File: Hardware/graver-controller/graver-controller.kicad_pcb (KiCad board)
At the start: 2 copper layers, 110 x 70 mm, 117 parts, among them J101 DC jack 5.5x2.1, J201 Handpiece, J301 USB-C, J302 SWD, J401 LCD XH 1x7, J402 NMJ6HCD2, Q101 DMP6023LE, Q201 IRLR3410, Q202 SI2309CDS, Q203 BSS123, SW301 BOOT0, SW302 RESET, SW401 EC11E15244G1, U101 LM5164DDAR, U102 AP2112K-3.3, U201 UCC27517DBVR, U202 TLV9062IDR, U301 STM32F411CEU6, U302 USBLC6-2SC6, U401 PESD5V0S2BT, Y301 25MHz 10pF

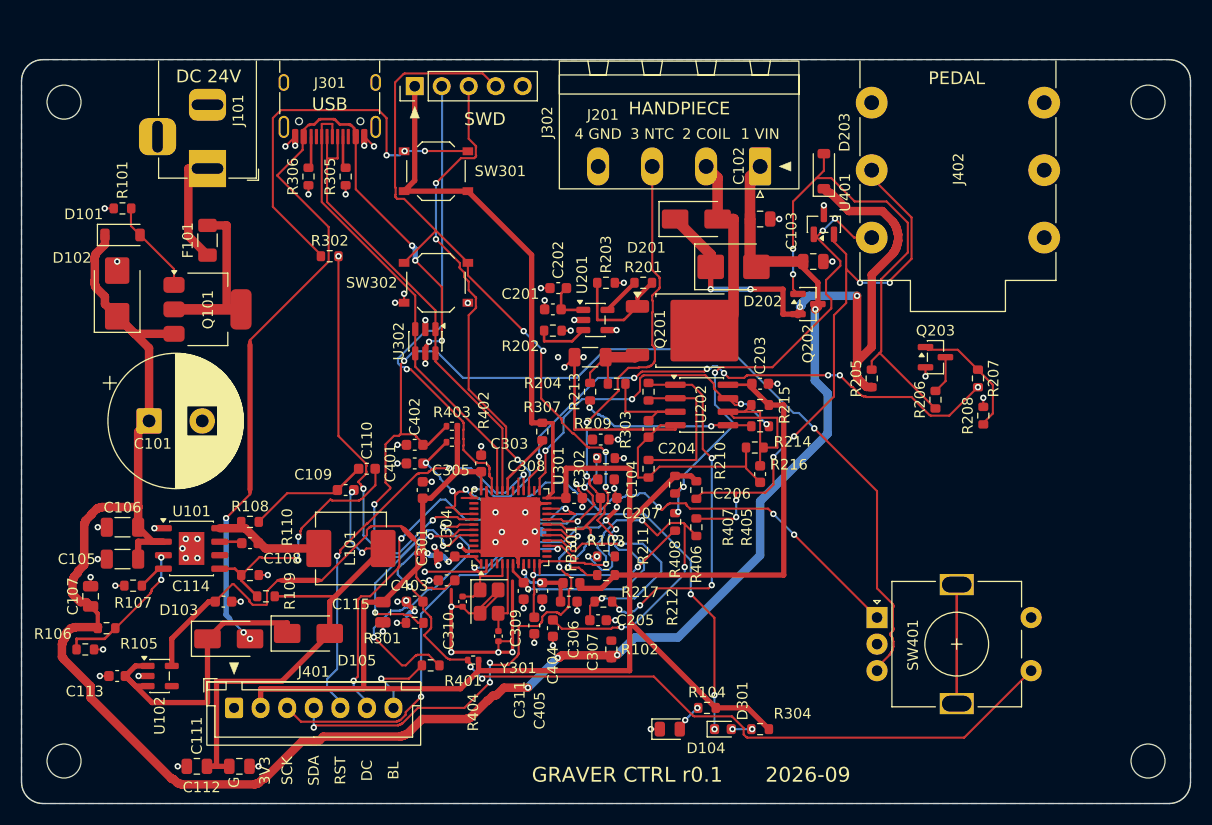
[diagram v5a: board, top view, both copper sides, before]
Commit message: hardware: GATE_IN, VCAP1 and VIN_SENSE drawn explicitly, 4 pad pairs left
copper.py: SIGNAL_EXPLICIT table drawn before the rails so the strike
signal (GATE_IN 16.7 mm), VCAP1 (10.8 mm) and the VIN_SENSE divider and
filter (20.2 mm, no via) get their lanes first. place.py: 3D model
substitutes for the QFN (EP 5.15 variant) and the two tact switches;
J301, SW401 and J402 have no library model anywhere and need
manufacturer STEP files before the enclosure export (README).

Repo board: 0 DRC errors, 0 parity, 4 unconnected pad pairs (I_SENSE x2,
DECAY_SLOW, LED_STAT), 202 vias. Budgets unchanged: USB 37.88/37.88
skew 0, flyback 21.4 mm, buck CIN 2.9/2.7 mm, Kelvin 1.15/1.23, sense
ground 5/5, no ADC net parallel to a switching net. +3V3 now 301 mm /
6 vias. An explicit I_SENSE trace was tried and reverted: it cost the
router GND and left 7 open.
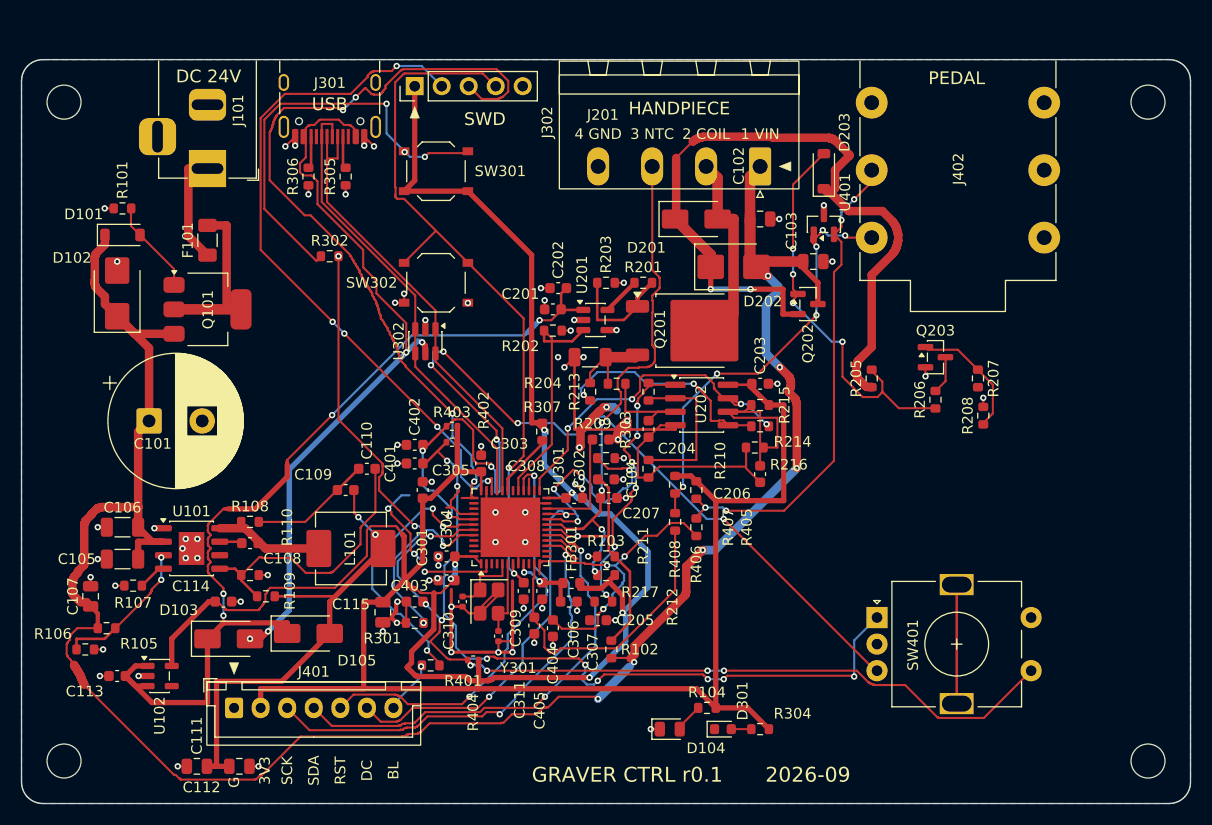
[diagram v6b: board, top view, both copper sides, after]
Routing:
- net +5V: track 33.2 -> 86.2 mm, vias 0 -> 4
- net DECAY_SLOW: track 52.4 -> 1.15 mm, vias 7 -> 0
- net LED_STAT: track 48.2 -> 6.56 mm, vias 5 -> 1
- net GND: track 193.6 -> 157.0 mm, vias 84 -> 82
- net SWCLK: track 52.2 -> 76.5 mm
- net +3V3: track 277.9 -> 301.0 mm, vias 2 -> 6
- net SWDIO: track 45.0 -> 66.3 mm, vias 1 -> 5
- net VIN_SENSE: track 3.15 -> 23.3 mm
- net I_SENSE: track 22.8 -> 3.01 mm, vias 2 -> 0
- net VBUS: track 89.6 -> 69.9 mm, vias 8 -> 4
- net NRST: track 87.8 -> 69.4 mm, vias 6 -> 2
- net ENC_A: track 59.8 -> 75.9 mm, vias 6 -> 8
- net GATE_IN: track 6.27 -> 21.8 mm
- net /Driver/CLAMP: track 57.9 -> 72.6 mm, vias 4 -> 2
- net Net-(U301-PB2): track 10.5 -> 22.3 mm, vias 3 -> 4
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
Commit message: hardware: scripted GND stitching, I_SENSE explicit, manual-track preservation
copper.py: every top-side GND pad (58) gets its own stub and via into
the pour, 17 edge stitching vias, a GND spine joining the F.Cu pieces;
the router no longer routes GND. Two real bugs fixed on the way: pad
numbers are not unique (SW302 has two pads '2', one was stitched twice
and one never) and the crystal's ground pads were tied to each other
and to nothing else. I_SENSE drawn explicitly (7.7 mm, no via).
manual.py + place.py --export-manual keep tracks drawn by hand in
pcbnew across regeneration (round trip verified, manual.json absent).

Repo board: 0 DRC errors, 0 parity, 5 unconnected pad pairs (GND x2
pour islands at C309/C205, ENC_B x2, +5V), 219 vias; one worse than
3406b49, the router's B.Cu tracks dice the pour. Budgets unchanged:
USB 37.88/37.88 skew 0, flyback 21.4 mm, buck CIN < 3 mm, Kelvin
1.15/1.23, sense ground 5/5, no ADC net parallel to a switching net.
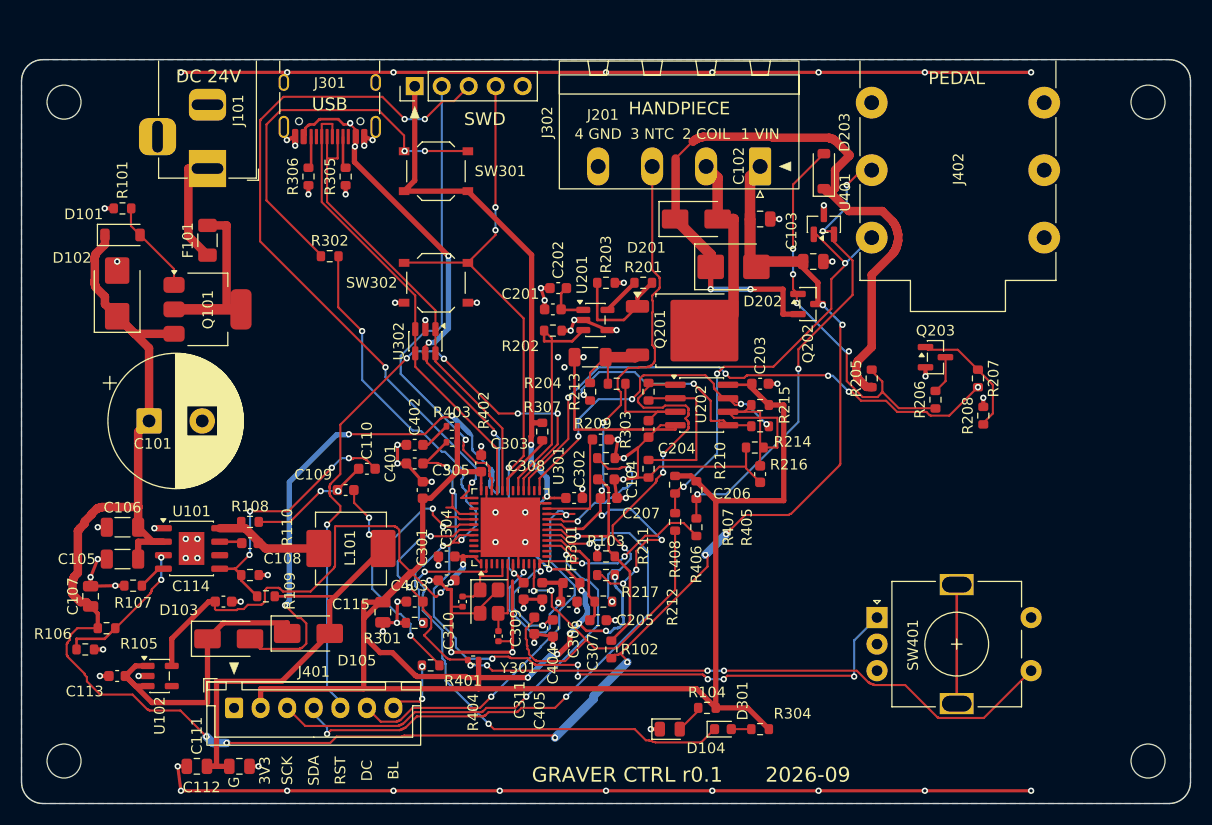
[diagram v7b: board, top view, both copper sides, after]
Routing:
- net GND: track 157.0 -> 308.6 mm, vias 82 -> 87
- net ENC_B: track 95.7 -> 5.62 mm, vias 8 -> 0
- net +5V: track 86.2 -> 33.2 mm, vias 4 -> 0
- net DECAY_SLOW: track 1.15 -> 53.1 mm, vias 0 -> 5
- net LED_STAT: track 6.56 -> 46.4 mm, vias 1 -> 2
- net VBUS: track 69.9 -> 96.9 mm, vias 4 -> 8
- net LCD_RST: track 39.8 -> 62.9 mm, vias 2 -> 5
- net SWDIO: track 66.3 -> 44.5 mm, vias 5 -> 1
- net NRST: track 69.4 -> 58.3 mm, vias 2 -> 4
- net LCD_MOSI: track 43.7 -> 54.6 mm, vias 2 -> 3
- net NTC: track 49.2 -> 59.4 mm, vias 4 -> 6
- net /MCU/VDDA: track 6.55 -> 16.3 mm
- net PEDAL_TIP: track 28.9 -> 37.2 mm, vias 0 -> 2
- net SWCLK: track 76.5 -> 68.3 mm
- net I_SENSE: track 3.01 -> 10.8 mm
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
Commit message: hardware: power widths honoured, GND closed, 3 pad pairs left
Two causes of the 0.2 mm power runs: the router necks a blocked wide
route down to --track-width and never widens it back, and the
.kicad_dru was never copied next to the scratch boards, so neither the
router nor the import gate saw the width rules (the real count was 237,
kicad-cli caps its report at 199). autoroute.py now routes one pass per
width floor (0.5, 0.3, then 0.2 mm signals), reads the floors from the
.kicad_dru and copies .kicad_pro + .kicad_dru beside every scratch
board; copper.py widths raised to the floors and checked.

Repo board with the width rules: 0 DRC errors, 0 parity, 3 unconnected
pad pairs (VDDA 2 mm, PB2 6 mm, +5V C201-D105 40 mm), 233 vias, all
GND pads on the main pour. Per-net minimum widths: VIN / CLAMP /
SHUNT_HI 0.5, COIL_NEG 1.0, +3V3 / +5V / VBUS / VDDA 0.3. Budgets
unchanged; +3V3 268 mm / 9 vias (was 300 / 13).
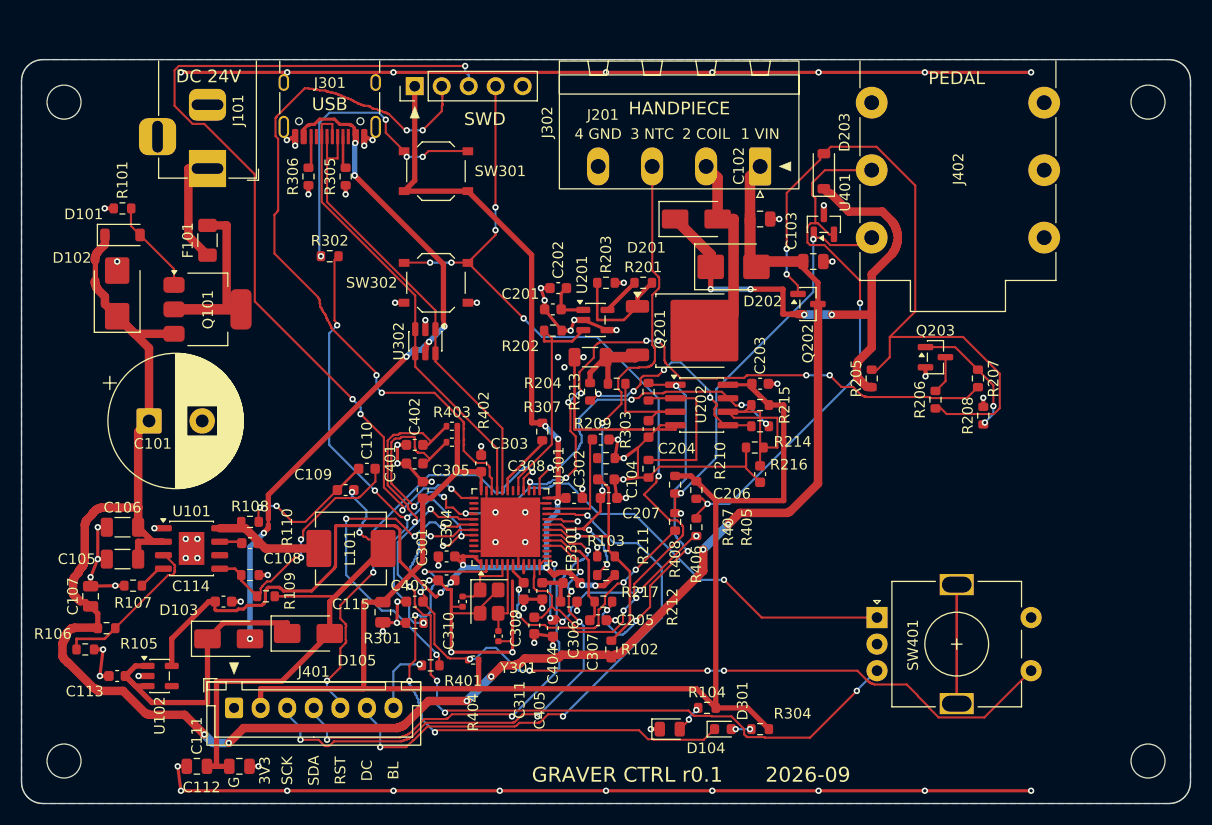
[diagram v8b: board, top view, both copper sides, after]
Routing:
- net ENC_B: track 5.62 -> 88.5 mm, vias 0 -> 6
- net +3V3: track 299.9 -> 267.9 mm, vias 13 -> 9
- net NRST: track 58.3 -> 89.5 mm, vias 4 -> 10
- net VBUS: track 96.9 -> 67.9 mm, vias 8 -> 7
- net Net-(D203-A): track 37.5 -> 66.4 mm, vias 4 -> 2
- net SWDIO: track 44.5 -> 68.0 mm, vias 1 -> 4
- net LCD_RST: track 62.9 -> 41.0 mm, vias 5 -> 3
- net /Driver/CLAMP: track 72.6 -> 51.4 mm, vias 2 -> 4
- net SWCLK: track 68.3 -> 88.7 mm, vias 4 -> 5
- net LCD_DC: track 39.0 -> 53.5 mm, vias 2 -> 3
- net PEDAL_TIP: track 37.2 -> 24.9 mm
- net /MCU/VDDA: track 16.3 -> 4.67 mm, vias 2 -> 0
- net Net-(U301-PB2): track 14.6 -> 2.98 mm, vias 2 -> 1
- net NTC: track 59.4 -> 48.8 mm, vias 6 -> 4
- net LCD_MOSI: track 54.6 -> 45.5 mm
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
